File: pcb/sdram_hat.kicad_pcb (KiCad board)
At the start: 2 copper layers, 76.2 x 76.2 mm, 25 parts, among them J1 CONN_02X20, J2 CONN_02X20, J3 CONN_02X20, J4 CONN_02X20, J5 AUDIO_OUT_JACK

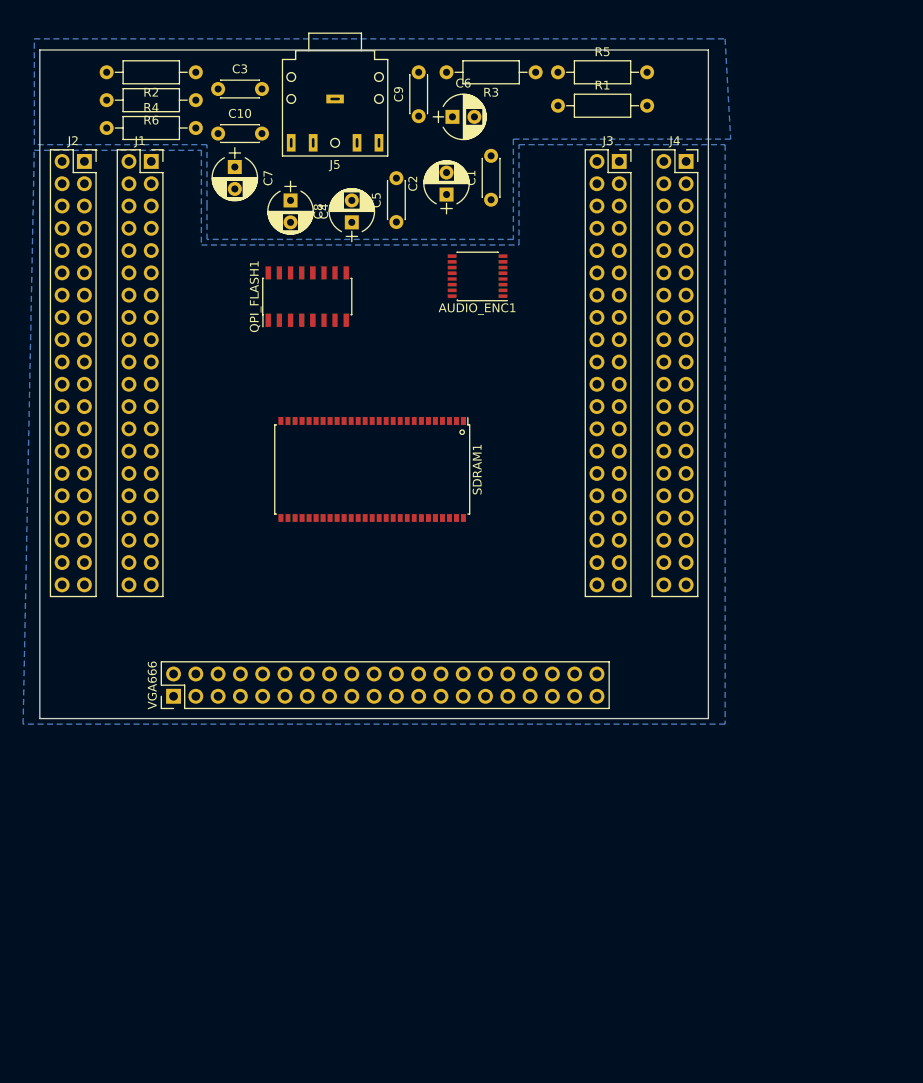
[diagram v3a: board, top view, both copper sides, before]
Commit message: Fixing AGND on a few DAC components
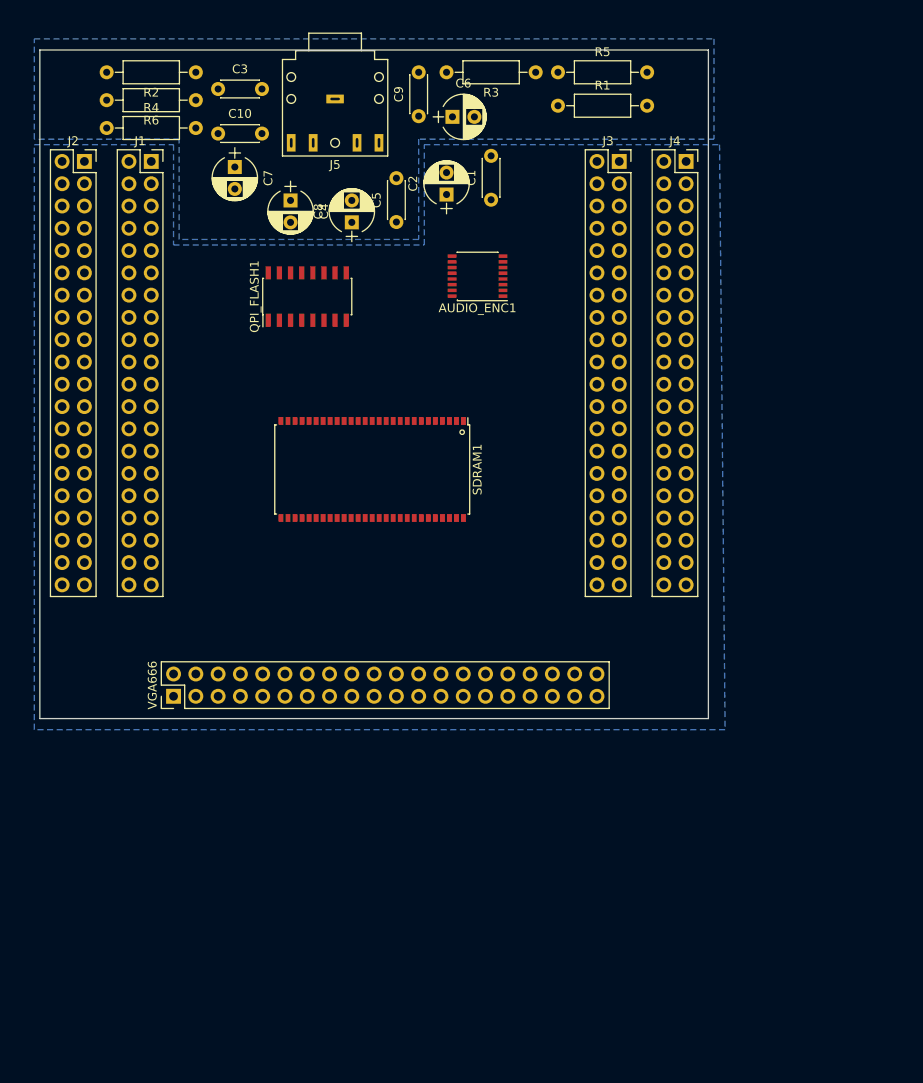
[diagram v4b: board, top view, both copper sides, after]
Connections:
- AUDIO_ENC1 pad 5: GNDA -> GND
- C1 pad 2: GNDA -> GND
- C10 pad 2: GND -> GNDA
- C2 pad 2: GNDA -> GND
- C9 pad 2: GND -> GNDA
- J1 pad 13: C9 -> (no net)
- J1 pad 17: B9 -> (no net)
- J1 pad 37: (no net) -> A1
- J2 pad 17: (no net) -> J14
- J2 pad 21: H14 -> (no net)
- J2 pad 28: (no net) -> G16
- J2 pad 30: (no net) -> F16
- J2 pad 34: E16 -> (no net)
- R3 pad 2: GND -> GNDA
- R4 pad 2: GND -> GNDA
- SDRAM1 pad 20: B9 -> A7
- SDRAM1 pad 21: C9 -> C7
- SDRAM1 pad 22: A7 -> B7
- SDRAM1 pad 23: F14 -> A6
- SDRAM1 pad 24: H14 -> C6
- SDRAM1 pad 25: G15 -> J14
- SDRAM1 pad 26: F15 -> F14
- SDRAM1 pad 29: B7 -> G16
- SDRAM1 pad 30: C7 -> F16
- SDRAM1 pad 31: A6 -> G15
- SDRAM1 pad 32: C6 -> F15
- VGA666 pad 7: E16 -> A1

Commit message: Moved to SMD, moving components to back side, added some decoupling
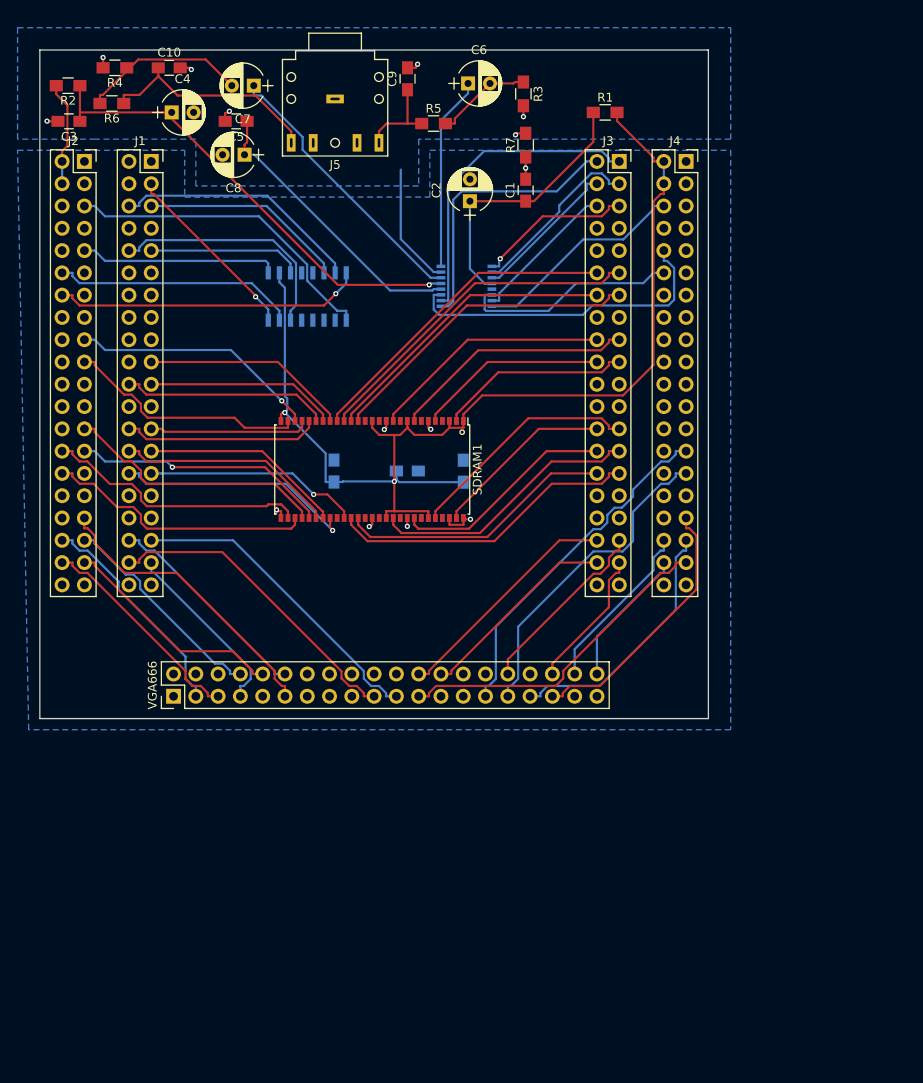
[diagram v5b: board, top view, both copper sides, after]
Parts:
- added C11: 100nF, Capacitors_SMD:C_0805_HandSoldering, B.Cu at (63.5, 63.2)
- added C12: 100nF, Capacitors_SMD:C_0805_HandSoldering, B.Cu at (57.1, 63.2)
- added C13: 100nF, Capacitors_SMD:C_0805_HandSoldering, B.Cu at (48.8, 63.2)
- added R7: 0, Resistors_SMD:R_0805_HandSoldering, F.Cu at (70.6, 26.1)
- AUDIO_ENC1, QPI_FLASH1: moved to B.Cu
- C1, C10, C3, C5, C9: footprint Capacitors_THT:C_Disc_D4.3mm_W1.9mm_P5.00mm -> Capacitors_SMD:C_0805_HandSoldering
- R1, R2, R3, R4, R5, R6: footprint Resistors_THT:R_Axial_DIN0207_L6.3mm_D2.5mm_P10.16mm_Horizontal -> Resistors_SMD:R_0805_HandSoldering
- moved C5 21.6 mm to (37.6, 23.4), turned to 180 degrees
- moved C3 17.4 mm to (18.6, 23.4), turned to 180 degrees
- moved C4 16.9 mm to (30.3, 22.4), turned to 0 degrees
- moved R5 15.3 mm to (60.1, 23.6)
- moved R2 14.6 mm to (18.5, 19.3)
- moved C8 14.5 mm to (38.6, 27.2), turned to 180 degrees
- moved R6 9.58 mm to (23.4, 21.3)
- moved C7 9.52 mm to (39.6, 19.3), turned to 180 degrees
- moved C10 9.34 mm to (30.0, 17.3)
- moved R4 6.92 mm to (23.8, 17.3), turned to 180 degrees
- moved R1 5.43 mm to (79.7, 22.4)
- moved C9 4.44 mm to (57.1, 18.5)
- moved C6 4.20 mm to (64.0, 19.1)
- moved C1 4.08 mm to (70.6, 31.2)
- moved R3 2.83 mm to (70.4, 20.2), turned to 270 degrees
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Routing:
- net +3V3: track 0.00 -> 131.5 mm, vias 0 -> 2
- net Net-(AUDIO_ENC1-Pad13): track 0.00 -> 54.1 mm, vias 0 -> 1
- net G1: track 0.00 -> 39.8 mm
- net M11: track 0.00 -> 39.0 mm
- net B2: track 0.00 -> 37.7 mm
- net F1: track 0.00 -> 37.2 mm
- net DAC_SFOR0: track 0.00 -> 37.2 mm
- net N10: track 0.00 -> 37.1 mm
- net P15: track 0.00 -> 36.9 mm
- net P10: track 0.00 -> 36.4 mm
- net A2: track 0.00 -> 36.1 mm
- net B3: track 0.00 -> 36.0 mm
- net DAC_PLL0: track 0.00 -> 35.7 mm
- net R5: track 0.00 -> 35.5 mm
- net K15: track 0.00 -> 35.3 mm, vias 0 -> 1
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
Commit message: Add a bunch of decoupling caps to PCB
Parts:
- added C14: 100nF, Capacitors_SMD:C_0805_HandSoldering, B.Cu at (42.7, 63.0)
- added C15: 100nF, Capacitors_SMD:C_0805_HandSoldering, B.Cu at (59.2, 63.0)
- added C16: 100nF, Capacitors_SMD:C_0805_HandSoldering, B.Cu at (57.2, 63.0)
- added C17: 100nF, Capacitors_SMD:C_0805_HandSoldering, B.Cu at (52.7, 63.0)
- added C18: 100nF, Capacitors_SMD:C_0805_HandSoldering, B.Cu at (54.7, 63.0)
- AUDIO_ENC1: footprint Housings_SSOP:SSOP-16_4.4x5.2mm_Pitch0.65mm -> pcb:SSOP-16_4.4x5.2mm_Pitch0.65mm_ExtendedPad
- C13: moved to F.Cu
- QPI_FLASH1: footprint Housings_SOIC:SOIC-16_3.9x9.9mm_Pitch1.27mm -> pcb:SOIC-16_3.9x9.9mm_Pitch1.27mm_ExtendedPad
- SDRAM1: footprint pcb:TSOPII-54_10.16x22.22mm-Pitch0.8mm -> pcb:TSOPII-54_10.16x22.22mm_Pitch0.8mm_ExtendedPad
- moved C13 20.3 mm to (45.7, 43.2), turned to 0 degrees
- moved C12 4.12 mm to (61.2, 63.0), turned to 90 degrees
- moved C11 0.37 mm to (63.2, 63.0), turned to 90 degrees
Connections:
- J1 pad 1: (no net) -> IO0
- J1 pad 11: (no net) -> B10
- J1 pad 12: (no net) -> A11
- J1 pad 13: (no net) -> C9
- J1 pad 14: (no net) -> A10
- J1 pad 17: (no net) -> B9
- J1 pad 18: (no net) -> A9
- J1 pad 2: (no net) -> A16
- J1 pad 20: (no net) -> B8
- J1 pad 33: (no net) -> C3
- J1 pad 34: (no net) -> B5
- J1 pad 4: (no net) -> A15
- J2 pad 1: (no net) -> IO1
- J2 pad 10: (no net) -> N16
- J2 pad 11: (no net) -> L16
- J2 pad 13: (no net) -> K16
- J2 pad 18: (no net) -> K14
- J2 pad 20: (no net) -> G14
- J2 pad 21: (no net) -> H14
- J2 pad 22: (no net) -> J15
- J2 pad 26: (no net) -> H16
- J2 pad 29: (no net) -> E14
- J2 pad 3: (no net) -> R15
- J2 pad 34: (no net) -> E16
- J2 pad 6: (no net) -> P16
- J3 pad 10: (no net) -> DAC_SFOR1
- J3 pad 21: (no net) -> R9
- J3 pad 22: (no net) -> T9
- J3 pad 33: (no net) -> R4
- J3 pad 34: (no net) -> R3
- J3 pad 6: DAC_SFOR1 -> T13
- J3 pad 9: (no net) -> P13
- J4 pad 1: (no net) -> IO3
- J4 pad 11: (no net) -> M1
- J4 pad 13: (no net) -> L1
- J4 pad 14: (no net) -> L3
- J4 pad 17: (no net) -> K1
- J4 pad 18: (no net) -> K3
- J4 pad 19: (no net) -> J1
- J4 pad 20: (no net) -> J2
- J4 pad 21: (no net) -> J3
- J4 pad 22: (no net) -> H2
- J4 pad 25: (no net) -> H1
- J4 pad 26: (no net) -> G2
- J4 pad 28: (no net) -> F2
- J4 pad 3: (no net) -> R1
- J4 pad 30: (no net) -> E2
- J4 pad 34: (no net) -> D1
- J4 pad 5: (no net) -> P2
- J4 pad 9: (no net) -> N2
- J5 pad 4: (no net) -> Net-(J5-Pad4)
- J5 pad 5: (no net) -> Net-(J5-Pad5)
- QPI_FLASH1 pad 16: B15 -> K15
- QPI_FLASH1 pad 8: K15 -> A16
- VGA666 pad 1: (no net) -> Net-(VGA666-Pad1)
- VGA666 pad 10: B16 -> C16
- VGA666 pad 13: (no net) -> Net-(VGA666-Pad13)
- VGA666 pad 15: (no net) -> Net-(VGA666-Pad15)
- VGA666 pad 16: (no net) -> Net-(VGA666-Pad16)
- VGA666 pad 17: (no net) -> Net-(VGA666-Pad17)
- VGA666 pad 18: (no net) -> Net-(VGA666-Pad18)
- VGA666 pad 2: (no net) -> Net-(VGA666-Pad2)
- VGA666 pad 22: (no net) -> Net-(VGA666-Pad22)
- VGA666 pad 27: (no net) -> Net-(VGA666-Pad27)
- VGA666 pad 28: (no net) -> Net-(VGA666-Pad28)
- VGA666 pad 37: (no net) -> Net-(VGA666-Pad37)
- VGA666 pad 4: (no net) -> Net-(VGA666-Pad4)
- VGA666 pad 5: C16 -> B16
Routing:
- net GNDA: track 23.3 -> 114.0 mm, vias 7 -> 0
- net GND: track 12.2 -> 92.4 mm, vias 7 -> 9
- net A16: track 0.00 -> 31.4 mm
- net B15: track 21.3 -> 0.00 mm, vias 1 -> 0
- net +3V3: track 131.5 -> 144.7 mm, vias 2 -> 9
- net DAC_BCK: track 18.0 -> 29.0 mm, vias 1 -> 0
- net K15: track 35.3 -> 25.8 mm, vias 1 -> 0
- net G16: track 30.2 -> 36.4 mm
- net DAC_SFOR0: track 37.2 -> 33.1 mm
- net Net-(C10-Pad1): track 25.8 -> 29.9 mm
- net DAC_PLL0: track 35.7 -> 31.9 mm, vias 0 -> 1
- net C16: track 25.0 -> 28.6 mm
- net C4: track 24.5 -> 27.7 mm
- net B16: track 26.0 -> 23.0 mm
- net B6: track 25.2 -> 28.1 mm, vias 0 -> 1
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- removed copper zone on B.Cu, net GNDA

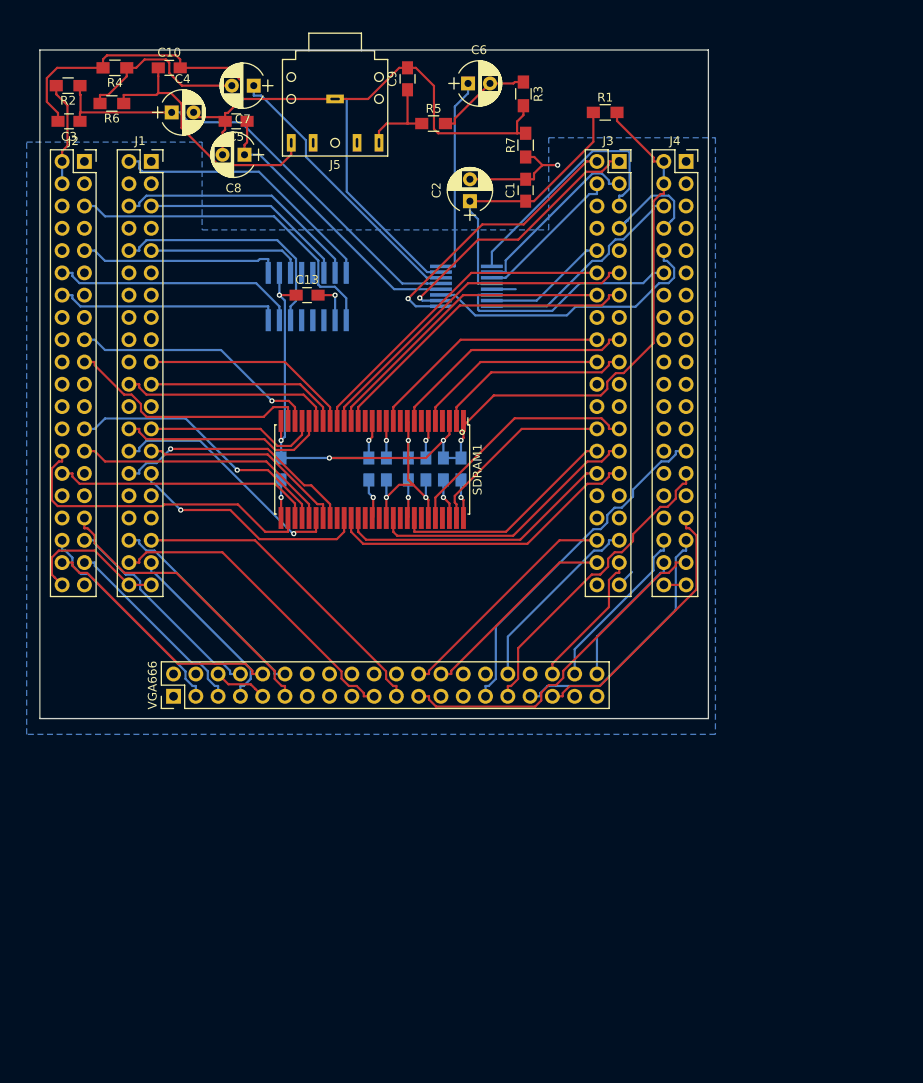
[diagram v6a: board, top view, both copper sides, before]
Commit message: Fix footprint size for SOIC package QPI flash
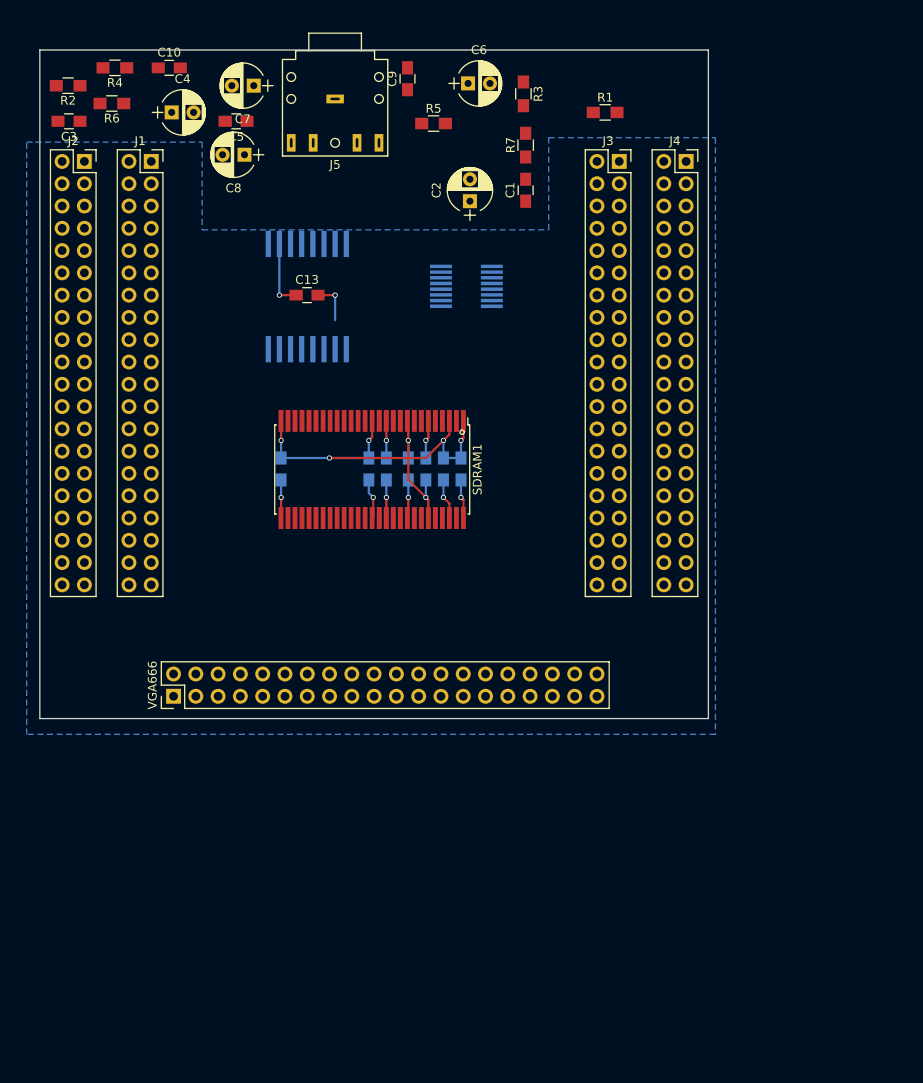
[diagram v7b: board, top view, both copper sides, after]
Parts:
- QPI_FLASH1: footprint pcb:SOIC-16_3.9x9.9mm_Pitch1.27mm_ExtendedPad -> pcb:SOIC-16_7.5x9.9mm_Pitch1.27mm_ExtendedPad
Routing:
- net GNDA: track 114.0 -> 0.00 mm
- net +3V3: track 144.7 -> 71.4 mm
- net GND: track 92.4 -> 35.8 mm, vias 9 -> 8
- net Net-(AUDIO_ENC1-Pad13): track 53.4 -> 0.00 mm
- net G1: track 39.8 -> 0.00 mm
- net M11: track 39.5 -> 0.00 mm
- net B2: track 39.2 -> 0.00 mm
- net P15: track 38.3 -> 0.00 mm
- net N10: track 37.5 -> 0.00 mm
- net P10: track 36.8 -> 0.00 mm
- net B3: track 36.5 -> 0.00 mm
- net G16: track 36.4 -> 0.00 mm
- net R5: track 36.2 -> 0.00 mm
- net A2: track 36.1 -> 0.00 mm
- net F1: track 35.8 -> 0.00 mm
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
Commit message: Attempt #2 at previous
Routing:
- net GNDA: track 0.00 -> 114.0 mm
- net +3V3: track 71.4 -> 149.4 mm
- net Net-(AUDIO_ENC1-Pad4): track 0.00 -> 66.0 mm
- net Net-(AUDIO_ENC1-Pad13): track 0.00 -> 53.4 mm
- net B12: track 0.00 -> 48.3 mm
- net P15: track 0.00 -> 41.9 mm
- net G1: track 0.00 -> 39.8 mm
- net M11: track 0.00 -> 39.5 mm
- net B2: track 0.00 -> 37.7 mm
- net N10: track 0.00 -> 37.5 mm
- net DAC_SFOR0: track 0.00 -> 37.2 mm
- net F1: track 0.00 -> 37.2 mm
- net P10: track 0.00 -> 36.8 mm
- net B3: track 0.00 -> 36.5 mm
- net G16: track 0.00 -> 36.4 mm
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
